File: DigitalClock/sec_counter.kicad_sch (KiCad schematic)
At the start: 43 parts

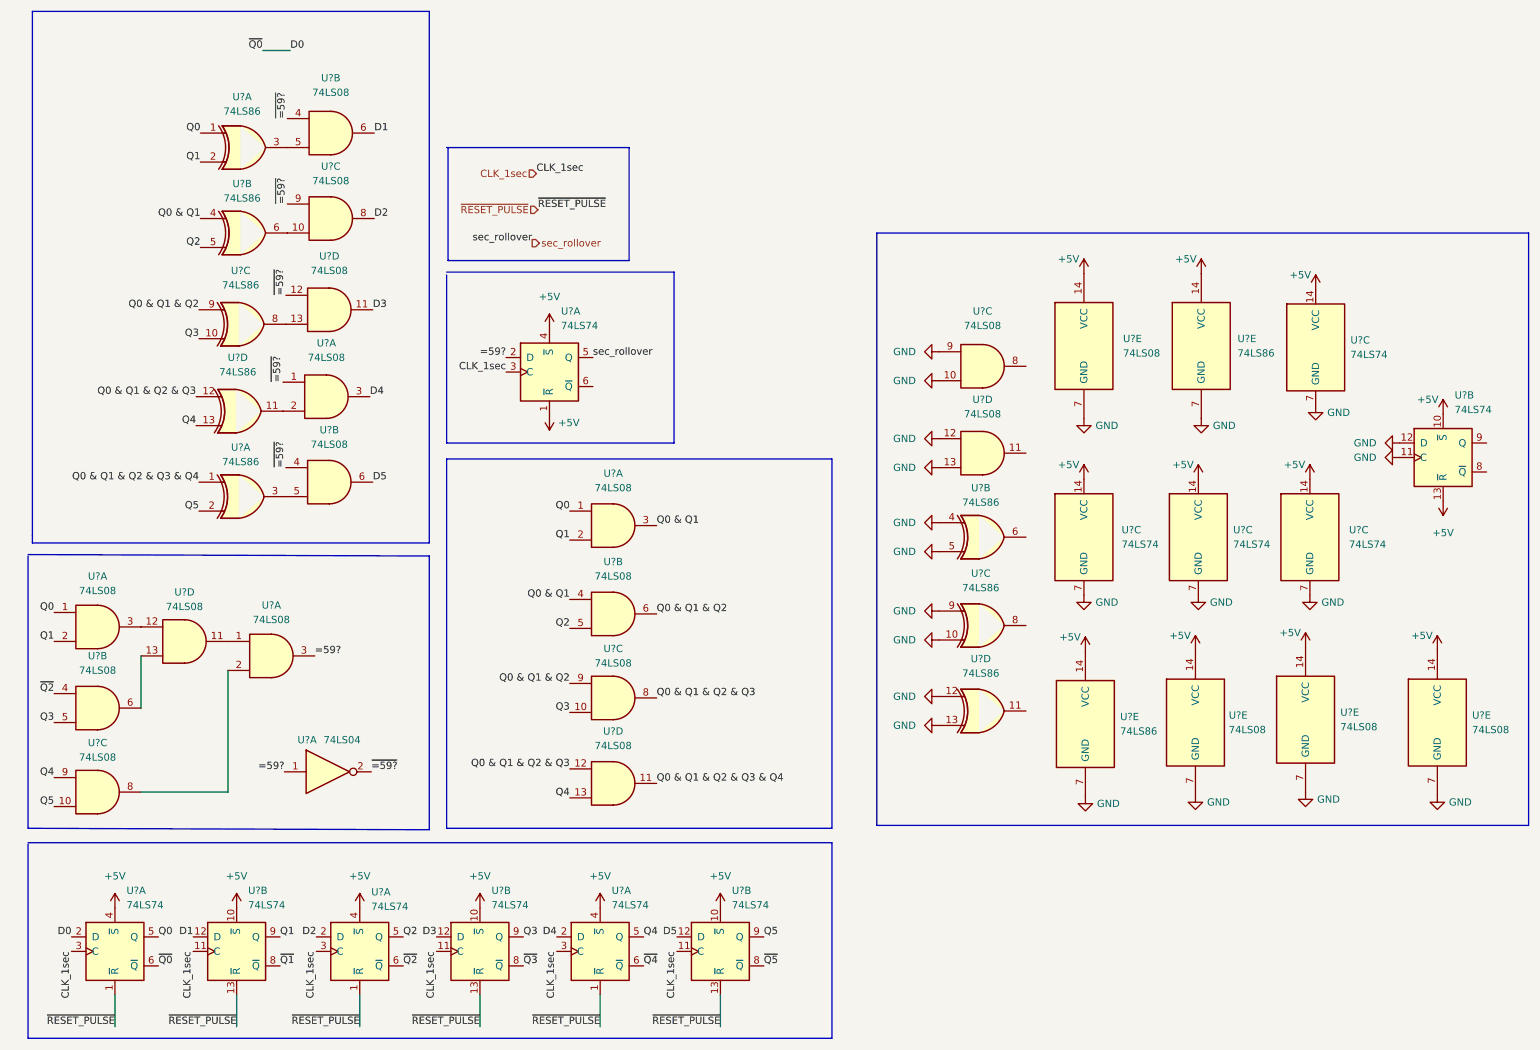
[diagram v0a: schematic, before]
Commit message: added minute counter schematic"
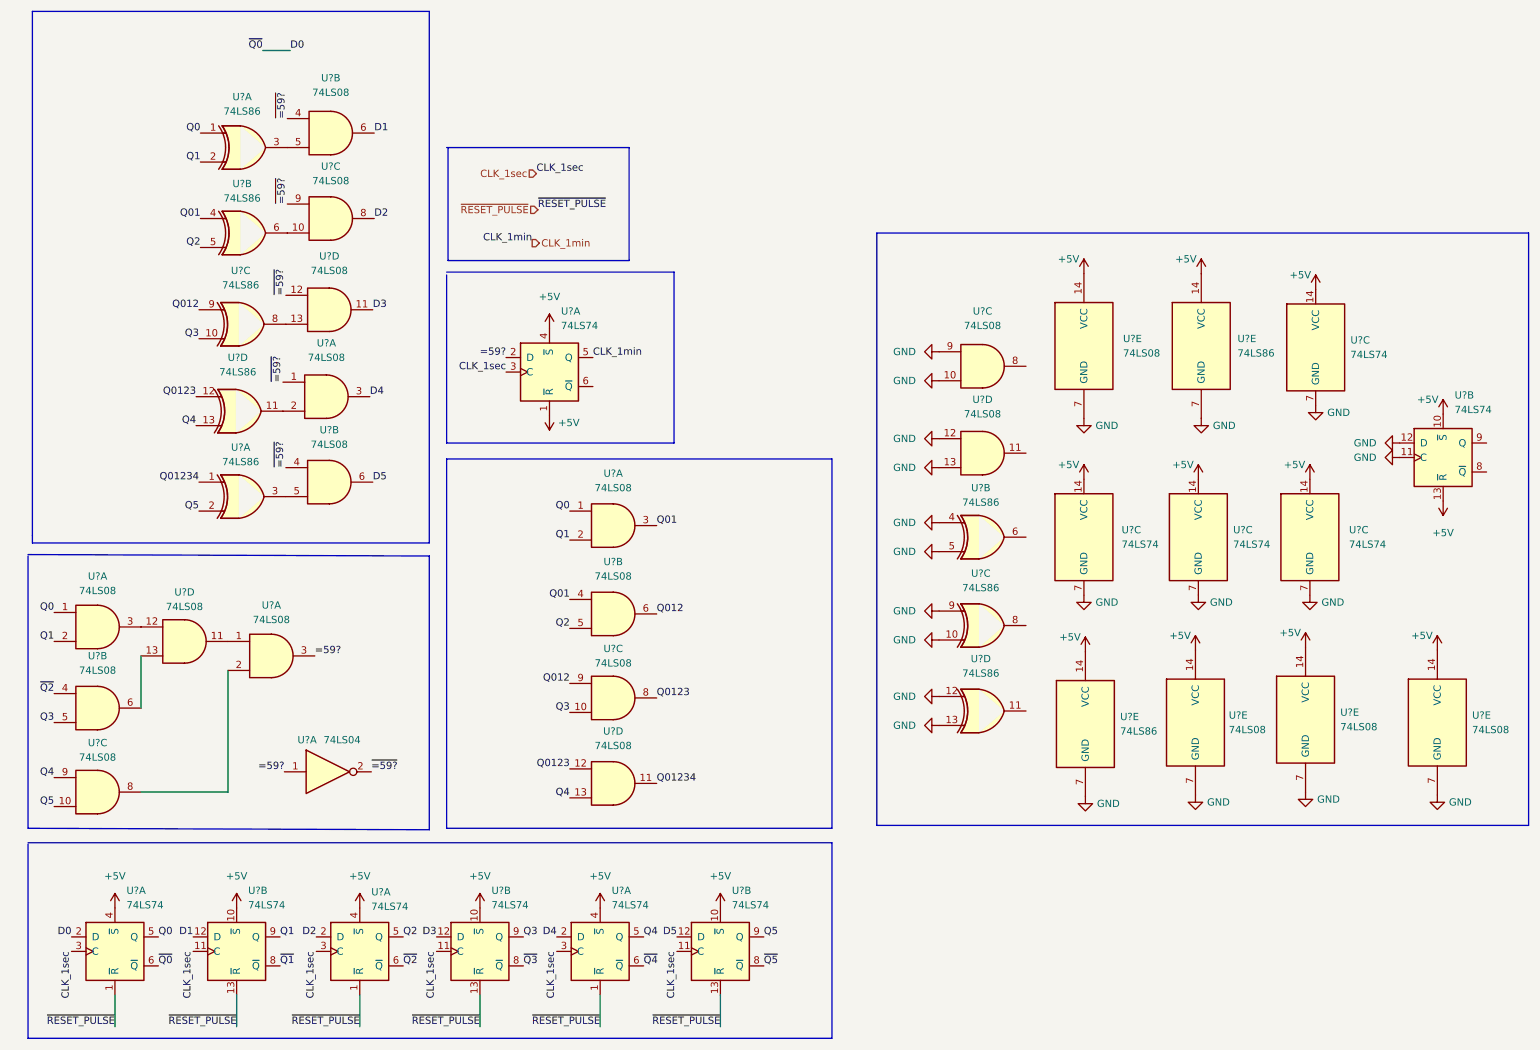
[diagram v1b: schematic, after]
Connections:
- net Q0 & Q1 renamed Q01
- net Q0 & Q1 & Q2 renamed Q012
- net Q0 & Q1 & Q2 & Q3 renamed Q0123
- net Q0 & Q1 & Q2 & Q3 & Q4 renamed Q01234
- net sec_rollover renamed CLK_1min
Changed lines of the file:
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@@
     (effects (font (size 1.27 1.27)) (justify left bottom))
   )
-  (label "Q0 & Q1 & Q2" (at 110.998 131.064 180)
+  (label "Q012" (at 110.998 131.064 180)
     (effects (font (size 1.27 1.27)) (justify right bottom))
   )
@@
     (effects (font (size 1.27 1.27)) (justify left bottom))
   )
-  (label "Q0 & Q1 & Q2 & Q3" (at 110.998 146.05 180)
+  (label "Q0123" (at 110.998 146.05 180)
     (effects (font (size 1.27 1.27)) (justify right bottom))
   )
@@
     (effects (font (size 1.27 1.27)) (justify right bottom))
   )
-  (label "Q0 & Q1 & Q2 & Q3" (at 126.238 133.604 0)
+  (label "Q0123" (at 126.238 133.604 0)
     (effects (font (size 1.27 1.27)) (justify left bottom))
   )
@@
     (effects (font (size 1.27 1.27)) (justify right bottom))
   )
+  (label "Q0123" (at 45.466 80.772 180)
+    (effects (font (size 1.27 1.27)) (justify right bottom))
+  )
+  (label "Q012" (at 45.974 65.532 180)
+    (effects (font (size 1.27 1.27)) (justify right bottom))
+  )
   (label "~{RESET_PULSE}" (at 95.25 191.262 180)
     (effects (font (size 1.27 1.27)) (justify right bottom))
@@
     (effects (font (size 1.27 1.27)) (justify right bottom))
   )
-  (label "sec_rollover" (at 104.394 53.848 180)
+  (label "CLK_1min" (at 104.394 53.848 180)
     (effects (font (size 1.27 1.27)) (justify right bottom))
   )
@@
     (effects (font (size 1.27 1.27)) (justify right bottom))
   )
-  (label "Q0 & Q1 & Q2" (at 126.238 118.872 0)
+  (label "Q012" (at 126.238 118.872 0)
     (effects (font (size 1.27 1.27)) (justify left bottom))
   )
@@
     (effects (font (size 1.27 1.27)) (justify right bottom))
   )
+  (label "Q01234" (at 45.974 95.758 180)
+    (effects (font (size 1.27 1.27)) (justify right bottom))
+  )
   (label "Q2" (at 46.228 54.61 180)
     (effects (font (size 1.27 1.27)) (justify right bottom))
@@
     (effects (font (size 1.27 1.27)) (justify left bottom))
   )
-  (label "Q0 & Q1 & Q2" (at 45.974 65.532 180)
-    (effects (font (size 1.27 1.27)) (justify right bottom))
-  )
   (label "D1" (at 76.708 34.544 0)
     (effects (font (size 1.27 1.27)) (justify left bottom))
@@
     (effects (font (size 1.27 1.27)) (justify left bottom))
   )
+  (label "Q01" (at 46.228 49.53 180)
+    (effects (font (size 1.27 1.27)) (justify right bottom))
+  )
   (label "CLK_1sec" (at 23.622 178.054 270)
     (effects (font (size 1.27 1.27)) (justify right bottom))
@@
     (effects (font (size 1.27 1.27)) (justify right bottom))
   )
-  (label "Q0 & Q1 & Q2 & Q3 & Q4" (at 126.238 148.59 0)
+  (label "Q01234" (at 126.238 148.59 0)
     (effects (font (size 1.27 1.27)) (justify left bottom))
   )
@@
     (effects (font (size 1.27 1.27)) (justify left bottom))
   )
-  (label "Q0 & Q1" (at 126.238 103.378 0)
+  (label "Q01" (at 126.238 103.378 0)
     (effects (font (size 1.27 1.27)) (justify left bottom))
   )
@@
     (effects (font (size 1.27 1.27)) (justify left bottom))
   )
-  (label "Q0 & Q1" (at 110.998 116.332 180)
+  (label "Q01" (at 110.998 116.332 180)
     (effects (font (size 1.27 1.27)) (justify right bottom))
   )
@@
     (effects (font (size 1.27 1.27)) (justify right bottom))
   )
-  (label "Q0 & Q1 & Q2 & Q3 & Q4" (at 45.974 95.758 180)
-    (effects (font (size 1.27 1.27)) (justify right bottom))
-  )
   (label "D5" (at 76.454 95.758 0)
     (effects (font (size 1.27 1.27)) (justify left bottom))
@@
     (effects (font (size 1.27 1.27)) (justify right bottom))
   )
-  (label "Q0 & Q1 & Q2 & Q3" (at 45.466 80.772 180)
-    (effects (font (size 1.27 1.27)) (justify right bottom))
-  )
   (label "~{Q0}" (at 38.862 180.594 0)
     (effects (font (size 1.27 1.27)) (justify left bottom))
   )
-  (label "sec_rollover" (at 115.062 73.914 0)
+  (label "CLK_1min" (at 115.062 73.914 0)
     (effects (font (size 1.27 1.27)) (justify left bottom))
   )
@@
     (effects (font (size 1.27 1.27)) (justify right bottom))
   )
-  (label "Q0 & Q1" (at 46.228 49.53 180)
-    (effects (font (size 1.27 1.27)) (justify right bottom))
-  )
   (label "~{Q3}" (at 102.87 180.594 0)
     (effects (font (size 1.27 1.27)) (justify left bottom))
@@
     (effects (font (size 1.27 1.27)) (justify right bottom))
   )
-  (hierarchical_label "sec_rollover" (shape output) (at 104.394 53.848 0)
+  (hierarchical_label "CLK_1min" (shape output) (at 104.394 53.848 0)
     (effects (font (size 1.27 1.27)) (justify left))
   )

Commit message: finished kicad schematic
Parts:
- gave numbers to parts that had none: 11
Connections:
- no-connect marks 0 -> 8

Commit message: about to begin layout
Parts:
- U15, U16, U17, U18, U19, U20, U21, U22, U23, U24, U25: footprint (none) -> Package_DIP:DIP-14_W7.62mm

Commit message: more routing
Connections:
- net +5V: now also U23.13 (~{R}); no longer U24.13 (~{R})
- net CLK_1sec: now also U24.11 (C); no longer U23.11 (C)
- net D5: now also U24.12 (D); no longer U23.12 (D)
- net GND: now also U23.11 (C), U23.12 (D); no longer U24.11 (C), U24.12 (D)
- net Q5: now also U24.9 (Q); no longer U23.9 (Q)
- net ~{Q5}: now also U24.8 (~{Q}); no longer U23.8 (~{Q})
- net ~{RESET_PULSE}: now also U24.13 (~{R}); no longer U23.13 (~{R})
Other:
- moved on the sheet: U23B, U24B
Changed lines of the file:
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@@
     (pin "1")
   )
-  (symbol (lib_id "74xx:74LS74") (at 264.16 91.44 0) (unit 2)
-    (in_bom yes) (on_board yes) (fields_autoplaced)
-    (property "Reference" "U24" (id 0) (at 266.1794 80.518 0)
-      (effects (font (size 1.27 1.27)) (justify left))
-    )
-    (property "Value" "74LS74" (id 1) (at 266.1794 83.058 0)
-      (effects (font (size 1.27 1.27)) (justify left))
-    )
-    (property "Footprint" "Package_DIP:DIP-14_W7.62mm" (id 2) (at 264.16 91.44 0)
-      (effects (font (size 1.27 1.27)) hide)
-    )
-    (property "Datasheet" "74xx/74hc_hct74.pdf" (id 3) (at 264.16 91.44 0)
+  (symbol (lib_id "74xx:74LS74") (at 137.414 178.054 0) (unit 2)
+    (in_bom yes) (on_board yes) (fields_autoplaced)
+    (property "Reference" "U24" (id 0) (at 139.4334 167.132 0)
+      (effects (font (size 1.27 1.27)) (justify left))
+    )
+    (property "Value" "74LS74" (id 1) (at 139.4334 169.672 0)
+      (effects (font (size 1.27 1.27)) (justify left))
+    )
+    (property "Footprint" "Package_DIP:DIP-14_W7.62mm" (id 2) (at 137.414 178.054 0)
+      (effects (font (size 1.27 1.27)) hide)
+    )
+    (property "Datasheet" "74xx/74hc_hct74.pdf" (id 3) (at 137.414 178.054 0)
       (effects (font (size 1.27 1.27)) hide)
     )
@@
     (pin "1")
   )
-  (symbol (lib_id "74xx:74LS74") (at 137.414 178.054 0) (unit 2)
-    (in_bom yes) (on_board yes) (fields_autoplaced)
-    (property "Reference" "U23" (id 0) (at 139.4334 167.386 0)
-      (effects (font (size 1.27 1.27)) (justify left))
-    )
-    (property "Value" "74LS74" (id 1) (at 139.4334 169.926 0)
-      (effects (font (size 1.27 1.27)) (justify left))
-    )
-    (property "Footprint" "Package_DIP:DIP-14_W7.62mm" (id 2) (at 137.414 178.054 0)
-      (effects (font (size 1.27 1.27)) hide)
-    )
-    (property "Datasheet" "74xx/74hc_hct74.pdf" (id 3) (at 137.414 178.054 0)
-      (effects (font (size 1.27 1.27)) hide)
-    )
+  (symbol (lib_id "74xx:74LS74") (at 264.16 91.44 0) (unit 2)
+    (in_bom yes) (on_board yes) (fields_autoplaced)
+    (property "Reference" "U23" (id 0) (at 266.1794 80.772 0)
+      (effects (font (size 1.27 1.27)) (justify left))
+    )
+    (property "Value" "74LS74" (id 1) (at 266.1794 83.312 0)
+      (effects (font (size 1.27 1.27)) (justify left))
+    )
+    (property "Footprint" "Package_DIP:DIP-14_W7.62mm" (id 2) (at 264.16 91.44 0)
+      (effects (font (size 1.27 1.27)) hide)
+    )
+    (property "Datasheet" "74xx/74hc_hct74.pdf" (id 3) (at 264.16 91.44 0)
+      (effects (font (size 1.27 1.27)) hide)
+    )

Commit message: started routing
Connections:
- net =59?: now also U21.6; no longer U20.3
- net D1: now also U20.3; no longer U21.6
- net D2: now also U20.6; no longer U20.8
- net D3: now also U20.8; no longer U20.11
- net D4: now also U20.11; no longer U21.3
- net D5: now also U21.3; no longer U20.6
- net GND: now also U21.10, U21.12, U21.13, U21.9; no longer U25.10, U25.12, U25.13, U25.9
- net Q0: now also U18.1; no longer U19.1
- net Q012: now also U25.9; no longer U21.9
- net Q0123: now also U25.12, U25.8; no longer U21.12, U21.8
- net Q01234: now also U19.1, U25.11; no longer U18.1, U21.11
- net Q1: now also U18.2; no longer U19.2
- net Q3: now also U25.10; no longer U21.10
- net Q4: now also U25.13; no longer U21.13
- net Q5: now also U19.2; no longer U18.2
- net ~{=59?}: now also U20.1; no longer U21.4
- net at U18.3: now also U20.2; no longer U20.5
- net at U16.11: now also U21.4; no longer U20.1
- net at U21.2: now also U19.3; no longer U18.11
- net at U20.10: now also U18.8; no longer U18.6
- net at U20.13: now also U18.11; no longer U18.8
- net at U21.5: now also U16.8; no longer U19.3
- new net: U18.6, U20.5
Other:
- moved on the sheet: U18A, U19A, U20A, U20B, U20C, U20D, U21A, U21B, U21C, U21D, U25C, U25D
